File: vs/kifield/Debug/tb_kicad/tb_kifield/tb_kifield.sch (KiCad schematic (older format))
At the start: 8 parts, among them U1 R

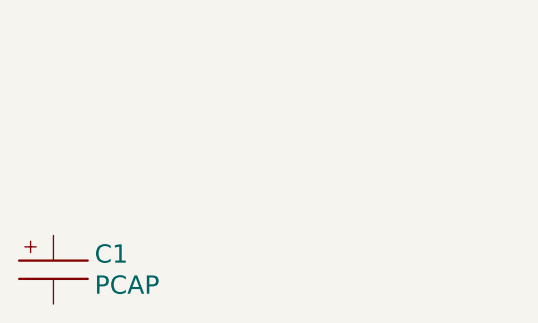
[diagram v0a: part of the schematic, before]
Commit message: Написал ReplaceAttr_text_size.bat для замены атрибута поля компонентов на 80.
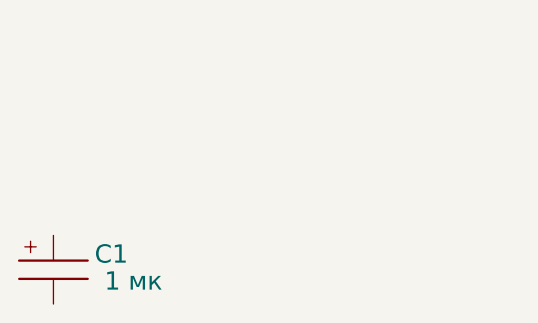
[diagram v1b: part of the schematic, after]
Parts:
- C1: Ном. - -> 1 мк
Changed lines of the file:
@@
 F 2 "-" H 9600 2085 40  0001 C CNN
 F 3 "-" H 9600 2085 40  0001 C CNN
-F 4 "-" H 9670 2085 40  0001 C CNN "Примечание"
-F 5 "-" H 9670 2085 40  0001 C CNN "Тип элемента"
-F 6 "-" H 9670 2085 40  0001 C CNN "Заказной номер "
-F 7 "-" H 9670 2085 40  0001 C CNN "Кол‐во"
-F 8 "-" H 9670 2085 40  0001 C CNN "Производитель"
-F 9 "-" H 9670 2085 40  0001 C CNN "Типоразмер"
-F 10 "-" H 9670 2085 40  0001 C CNN "Ном."
-F 11 "-" H 9670 2085 40  0001 C CNN "Откл,%"
+F 4 "-" H 9670 2085 40  0001 C CNN "Заказной номер "
+F 5 "-" H 9670 2085 40  0001 C CNN "Кол‐во"
+F 6 "-" H 9670 2085 40  0001 C CNN "Наименование 1С8 УПП"
+F 7 "-" H 9670 2085 40  0001 C CNN "Напр."
+F 8 "-" H 9670 2085 40  0001 C CNN "Ном."
+F 9 "-" H 9670 2085 40  0001 C CNN "Откл,%"
+F 10 "-" H 9670 2085 40  0001 C CNN "Примечание"
+F 11 "-" H 9670 2085 40  0001 C CNN "Производитель"
 F 12 "-" H 9670 2085 40  0001 C CNN "ТКЕ/ТКС"
-F 13 "-" H 9670 2085 40  0001 C CNN "Напр."
-F 14 "-" H 9670 2085 40  0001 C CNN "Наименование 1С8 УПП"
+F 13 "-" H 9670 2085 40  0001 C CNN "Тип элемента"
+F 14 "-" H 9670 2085 40  0001 C CNN "Типоразмер"
 	1    9600 2100
 	1    0    0    -1
@@
 F 2 "-" H 7650 2335 40  0001 C CNN
 F 3 "-" H 7650 2335 40  0001 C CNN
-F 4 "-" H 7650 2335 40  0001 C CNN "Примечание"
-F 5 "-" H 7650 2335 40  0001 C CNN "Тип элемента"
-F 6 "-" H 7650 2335 40  0001 C CNN "Заказной номер "
-F 7 "-" H 7650 2335 40  0001 C CNN "Кол‐во"
-F 8 "-" H 7650 2335 40  0001 C CNN "Производитель"
-F 9 "-" H 7650 2335 40  0001 C CNN "Типоразмер"
-F 10 "-" H 7650 2335 40  0001 C CNN "Ном."
-F 11 "-" H 7650 2335 40  0001 C CNN "Откл,%"
+F 4 "-" H 7650 2335 40  0001 C CNN "Заказной номер "
+F 5 "-" H 7650 2335 40  0001 C CNN "Кол‐во"
+F 6 "-" H 7650 2335 40  0001 C CNN "Наименование 1С8 УПП"
+F 7 "-" H 7650 2335 40  0001 C CNN "Напр."
+F 8 "-" H 7650 2335 40  0001 C CNN "Ном."
+F 9 "-" H 7650 2335 40  0001 C CNN "Откл,%"
+F 10 "-" H 7650 2335 40  0001 C CNN "Примечание"
+F 11 "-" H 7650 2335 40  0001 C CNN "Производитель"
 F 12 "-" H 7650 2335 40  0001 C CNN "ТКЕ/ТКС"
-F 13 "-" H 7650 2335 40  0001 C CNN "Напр."
-F 14 "-" H 7650 2335 40  0001 C CNN "Наименование 1С8 УПП"
+F 13 "-" H 7650 2335 40  0001 C CNN "Тип элемента"
+F 14 "-" H 7650 2335 40  0001 C CNN "Типоразмер"
 	1    7650 2350
 	1    0    0    -1
@@
 F 2 "-" H 7200 1600 30  0001 C CNN
 F 3 "-" H 7200 1600 30  0001 C CNN
-F 4 "-" H 7200 1600 30  0001 C CNN "Примечание"
-F 5 "-" H 7200 1600 30  0001 C CNN "Тип элемента"
-F 6 "-" H 7200 1600 30  0001 C CNN "Заказной номер "
-F 7 "-" H 7200 1600 30  0001 C CNN "Кол‐во"
-F 8 "-" H 7200 1600 30  0001 C CNN "Производитель"
-F 9 "-" H 7200 1600 30  0001 C CNN "Типоразмер"
-F 10 "-" H 7200 1600 30  0001 C CNN "Ном."
-F 11 "-" H 7200 1600 30  0001 C CNN "Откл,%"
+F 4 "-" H 7200 1600 30  0001 C CNN "Заказной номер "
+F 5 "-" H 7200 1600 30  0001 C CNN "Кол‐во"
+F 6 "-" H 7200 1600 30  0001 C CNN "Наименование 1С8 УПП"
+F 7 "-" H 7200 1600 30  0001 C CNN "Напр."
+F 8 "-" H 7200 1600 30  0001 C CNN "Ном."
+F 9 "-" H 7200 1600 30  0001 C CNN "Откл,%"
+F 10 "-" H 7200 1600 30  0001 C CNN "Примечание"
+F 11 "-" H 7200 1600 30  0001 C CNN "Производитель"
 F 12 "-" H 7200 1600 30  0001 C CNN "ТКЕ/ТКС"
-F 13 "-" H 7200 1600 30  0001 C CNN "Напр."
-F 14 "-" H 7200 1600 30  0001 C CNN "Наименование 1С8 УПП"
+F 13 "-" H 7200 1600 30  0001 C CNN "Тип элемента"
+F 14 "-" H 7200 1600 30  0001 C CNN "Типоразмер"
 	1    7200 1650
 	1    0    0    -1
@@
 F 2 "-" H 5600 1100 30  0001 C CNN
 F 3 "-" H 5600 1100 30  0001 C CNN
-F 4 "-" H 5600 1100 30  0001 C CNN "Примечание"
-F 5 "-" H 5600 1100 30  0001 C CNN "Тип элемента"
-F 6 "-" H 5600 1100 30  0001 C CNN "Заказной номер "
-F 7 "-" H 5600 1100 30  0001 C CNN "Кол‐во"
-F 8 "-" H 5600 1100 30  0001 C CNN "Производитель"
-F 9 "-" H 5600 1100 30  0001 C CNN "Типоразмер"
-F 10 "-" H 5600 1100 30  0001 C CNN "Ном."
-F 11 "-" H 5600 1100 30  0001 C CNN "Откл,%"
+F 4 "-" H 5600 1100 30  0001 C CNN "Заказной номер "
+F 5 "-" H 5600 1100 30  0001 C CNN "Кол‐во"
+F 6 "-" H 5600 1100 30  0001 C CNN "Наименование 1С8 УПП"
+F 7 "-" H 5600 1100 30  0001 C CNN "Напр."
+F 8 "-" H 5600 1100 30  0001 C CNN "Ном."
+F 9 "-" H 5600 1100 30  0001 C CNN "Откл,%"
+F 10 "-" H 5600 1100 30  0001 C CNN "Примечание"
+F 11 "-" H 5600 1100 30  0001 C CNN "Производитель"
 F 12 "-" H 5600 1100 30  0001 C CNN "ТКЕ/ТКС"
-F 13 "-" H 5600 1100 30  0001 C CNN "Напр."
-F 14 "-" H 5600 1100 30  0001 C CNN "Наименование 1С8 УПП"
+F 13 "-" H 5600 1100 30  0001 C CNN "Тип элемента"
+F 14 "-" H 5600 1100 30  0001 C CNN "Типоразмер"
 	1    5600 1500
 	1    0    0    -1
@@
 F 2 "-" H 7550 3350 30  0001 C CNN
 F 3 "-" H 7550 3350 30  0001 C CNN
-F 4 "-" H 7550 3350 30  0001 C CNN "Примечание"
-F 5 "-" H 7550 3350 30  0001 C CNN "Тип элемента"
-F 6 "-" H 7550 3350 30  0001 C CNN "Заказной номер "
-F 7 "-" H 7550 3350 30  0001 C CNN "Кол‐во"
-F 8 "-" H 7550 3350 30  0001 C CNN "Производитель"
-F 9 "-" H 7550 3350 30  0001 C CNN "Типоразмер"
-F 10 "-" H 7550 3350 30  0001 C CNN "Ном."
-F 11 "-" H 7550 3350 30  0001 C CNN "Откл,%"
+F 4 "-" H 7550 3350 30  0001 C CNN "Заказной номер "
+F 5 "-" H 7550 3350 30  0001 C CNN "Кол‐во"
+F 6 "-" H 7550 3350 30  0001 C CNN "Наименование 1С8 УПП"
+F 7 "-" H 7550 3350 30  0001 C CNN "Напр."
+F 8 "-" H 7550 3350 30  0001 C CNN "Ном."
+F 9 "-" H 7550 3350 30  0001 C CNN "Откл,%"
+F 10 "-" H 7550 3350 30  0001 C CNN "Примечание"
+F 11 "-" H 7550 3350 30  0001 C CNN "Производитель"
 F 12 "-" H 7550 3350 30  0001 C CNN "ТКЕ/ТКС"
-F 13 "-" H 7550 3350 30  0001 C CNN "Напр."
-F 14 "-" H 7550 3350 30  0001 C CNN "Наименование 1С8 УПП"
+F 13 "-" H 7550 3350 30  0001 C CNN "Тип элемента"
+F 14 "-" H 7550 3350 30  0001 C CNN "Типоразмер"
 	1    7550 3400
 	1    0    0    -1
@@
 P 2350 4150
 F 0 "C1" H 2530 4218 80  0000 L CNN
-F 1 "PCAP" H 2530 4082 80  0000 L CNN
+F 1 "PCAP" H 2530 4082 80  0001 L CNN
 F 2 "-" H 2350 4135 40  0001 C CNN
 F 3 "-" H 2350 4135 40  0001 C CNN
-F 4 "-" H 2420 4135 40  0001 C CNN "Примечание"
-F 5 "-" H 2420 4135 40  0001 C CNN "Тип элемента"
-F 6 "-" H 2420 4135 40  0001 C CNN "Заказной номер "
-F 7 "-" H 2420 4135 40  0001 C CNN "Кол‐во"
-F 8 "-" H 2420 4135 40  0001 C CNN "Производитель"
-F 9 "-" H 2420 4135 40  0001 C CNN "Типоразмер"
-F 10 "-" H 2420 4135 40  0001 C CNN "Ном."
-F 11 "-" H 2420 4135 40  0001 C CNN "Откл,%"
+F 4 "-" H 2420 4135 40  0001 C CNN "Заказной номер "
+F 5 "-" H 2420 4135 40  0001 C CNN "Кол‐во"
+F 6 "-" H 2420 4135 40  0001 C CNN "Наименование 1С8 УПП"
+F 7 "-" H 2420 4135 40  0001 C CNN "Напр."
+F 8 "1 мк" H 2700 4100 80  0000 C CNN "Ном."
+F 9 "-" H 2420 4135 40  0001 C CNN "Откл,%"
+F 10 "-" H 2420 4135 40  0001 C CNN "Примечание"
+F 11 "-" H 2420 4135 40  0001 C CNN "Производитель"
 F 12 "-" H 2420 4135 40  0001 C CNN "ТКЕ/ТКС"
-F 13 "-" H 2420 4135 40  0001 C CNN "Напр."
-F 14 "-" H 2420 4135 40  0001 C CNN "Наименование 1С8 УПП"
+F 13 "-" H 2420 4135 40  0001 C CNN "Тип элемента"
+F 14 "-" H 2420 4135 40  0001 C CNN "Типоразмер"
 	1    2350 4150
 	1    0    0    -1
@@
 F 2 "-" H 3000 1800 30  0001 C CNN
 F 3 "-" H 3000 1800 30  0001 C CNN
-F 4 "-" H 3000 1800 30  0001 C CNN "Примечание"
-F 5 "-" H 3000 1800 30  0001 C CNN "Тип элемента"
-F 6 "-" H 3000 1800 30  0001 C CNN "Заказной номер "
-F 7 "-" H 3000 1800 30  0001 C CNN "Кол‐во"
-F 8 "-" H 3000 1800 30  0001 C CNN "Производитель"
-F 9 "-" H 3000 1800 30  0001 C CNN "Типоразмер"
-F 10 "-" H 3000 1800 30  0001 C CNN "Ном."
-F 11 "-" H 3000 1800 30  0001 C CNN "Откл,%"
+F 4 "-" H 3000 1800 30  0001 C CNN "Заказной номер "
+F 5 "-" H 3000 1800 30  0001 C CNN "Кол‐во"
+F 6 "-" H 3000 1800 30  0001 C CNN "Наименование 1С8 УПП"
+F 7 "-" H 3000 1800 30  0001 C CNN "Напр."
+F 8 "-" H 3000 1800 30  0001 C CNN "Ном."
+F 9 "-" H 3000 1800 30  0001 C CNN "Откл,%"
+F 10 "-" H 3000 1800 30  0001 C CNN "Примечание"
+F 11 "-" H 3000 1800 30  0001 C CNN "Производитель"
 F 12 "-" H 3000 1800 30  0001 C CNN "ТКЕ/ТКС"
-F 13 "-" H 3000 1800 30  0001 C CNN "Напр."
-F 14 "-" H 3000 1800 30  0001 C CNN "Наименование 1С8 УПП"
+F 13 "-" H 3000 1800 30  0001 C CNN "Тип элемента"
+F 14 "-" H 3000 1800 30  0001 C CNN "Типоразмер"
 	1    3000 1850
 	1    0    0    -1
@@
 F 2 "-" H 4000 2400 30  0001 C CNN
 F 3 "-" H 4000 2400 30  0001 C CNN
-F 4 "-" H 4000 2400 30  0001 C CNN "Примечание"
-F 5 "-" H 4000 2400 30  0001 C CNN "Тип элемента"
-F 6 "-" H 4000 2400 30  0001 C CNN "Заказной номер "
-F 7 "-" H 4000 2400 30  0001 C CNN "Кол‐во"
-F 8 "-" H 4000 2400 30  0001 C CNN "Производитель"
-F 9 "-" H 4000 2400 30  0001 C CNN "Типоразмер"
-F 10 "-" H 4000 2400 30  0001 C CNN "Ном."
-F 11 "-" H 4000 2400 30  0001 C CNN "Откл,%"
+F 4 "-" H 4000 2400 30  0001 C CNN "Заказной номер "
+F 5 "-" H 4000 2400 30  0001 C CNN "Кол‐во"
+F 6 "-" H 4000 2400 30  0001 C CNN "Наименование 1С8 УПП"
+F 7 "-" H 4000 2400 30  0001 C CNN "Напр."
+F 8 "-" H 4000 2400 30  0001 C CNN "Ном."
+F 9 "-" H 4000 2400 30  0001 C CNN "Откл,%"
+F 10 "-" H 4000 2400 30  0001 C CNN "Примечание"
+F 11 "-" H 4000 2400 30  0001 C CNN "Производитель"
 F 12 "-" H 4000 2400 30  0001 C CNN "ТКЕ/ТКС"
-F 13 "-" H 4000 2400 30  0001 C CNN "Напр."
-F 14 "-" H 4000 2400 30  0001 C CNN "Наименование 1С8 УПП"
+F 13 "-" H 4000 2400 30  0001 C CNN "Тип элемента"
+F 14 "-" H 4000 2400 30  0001 C CNN "Типоразмер"
 	1    4000 2450
 	1    0    0    -1

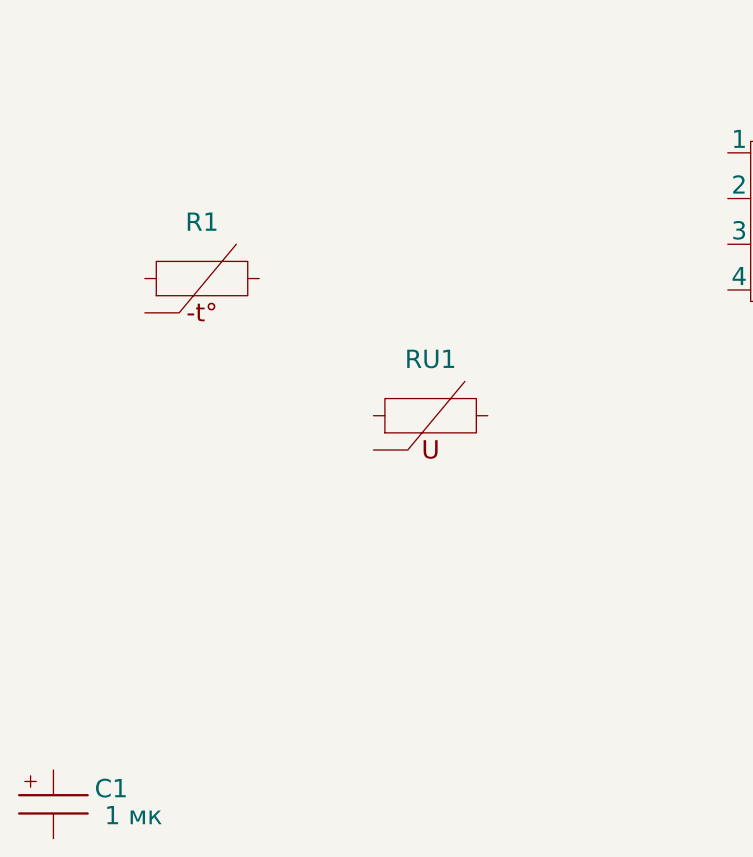
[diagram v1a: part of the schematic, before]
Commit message: Отладил ReplaceAttr_text_size.bat. Необходимо провести замены в файле Sch.tsv Refs -> Поз.обозначение value -> Наименование
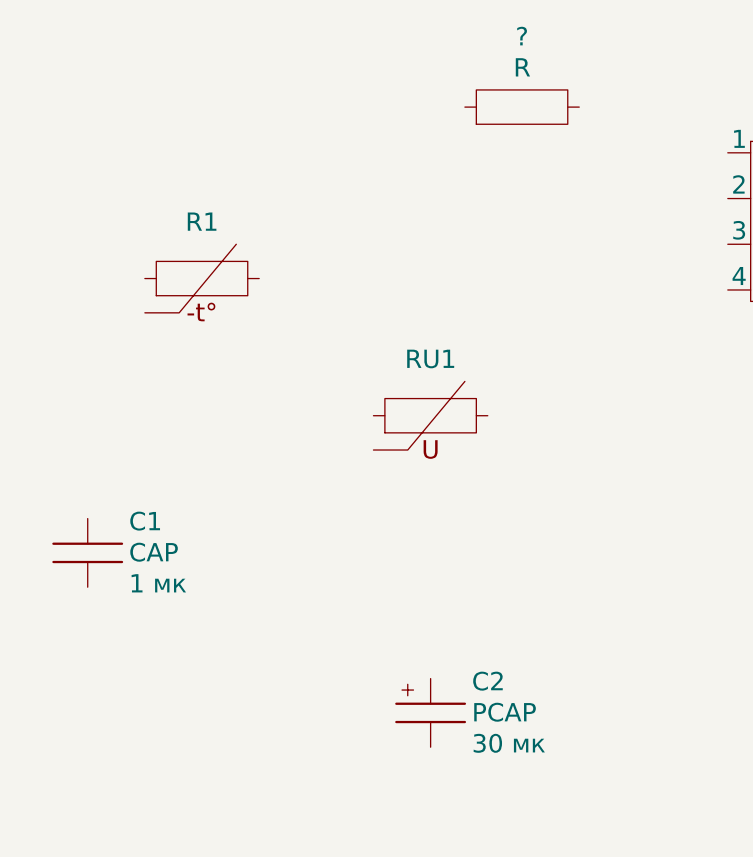
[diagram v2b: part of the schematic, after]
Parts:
- removed C1: PCAP, -, symbol Capacity:PCAP
- added ?: R, -, symbol Resistors:R
- added C1: CAP, -, symbol Capacity:CAP
- added C2: PCAP, -, symbol Capacity:PCAP
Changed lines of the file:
@@
-$EndComp
-$Comp
-L Capacity:PCAP C1
-U 1 1 5F918A9B
-P 2350 4150
-F 0 "C1" H 2530 4218 80  0000 L CNN
-F 1 "PCAP" H 2530 4082 80  0001 L CNN
-F 2 "-" H 2350 4135 40  0001 C CNN
-F 3 "-" H 2350 4135 40  0001 C CNN
-F 4 "-" H 2420 4135 40  0001 C CNN "Заказной номер "
-F 5 "-" H 2420 4135 40  0001 C CNN "Кол‐во"
-F 6 "-" H 2420 4135 40  0001 C CNN "Наименование 1С8 УПП"
-F 7 "-" H 2420 4135 40  0001 C CNN "Напр."
-F 8 "1 мк" H 2700 4100 80  0000 C CNN "Ном."
-F 9 "-" H 2420 4135 40  0001 C CNN "Откл,%"
-F 10 "-" H 2420 4135 40  0001 C CNN "Примечание"
-F 11 "-" H 2420 4135 40  0001 C CNN "Производитель"
-F 12 "-" H 2420 4135 40  0001 C CNN "ТКЕ/ТКС"
-F 13 "-" H 2420 4135 40  0001 C CNN "Тип элемента"
-F 14 "-" H 2420 4135 40  0001 C CNN "Типоразмер"
-	1    2350 4150
-	1    0    0    -1
 $EndComp
 $Comp
@@
 F 0 "RU1" H 4000 2696 80  0000 C CNN
 F 1 "RU" H 4000 2200 80  0001 C CNN
-F 2 "-" H 4000 2400 30  0001 C CNN
-F 3 "-" H 4000 2400 30  0001 C CNN
-F 4 "-" H 4000 2400 30  0001 C CNN "Заказной номер "
-F 5 "-" H 4000 2400 30  0001 C CNN "Кол‐во"
-F 6 "-" H 4000 2400 30  0001 C CNN "Наименование 1С8 УПП"
-F 7 "-" H 4000 2400 30  0001 C CNN "Напр."
-F 8 "-" H 4000 2400 30  0001 C CNN "Ном."
-F 9 "-" H 4000 2400 30  0001 C CNN "Откл,%"
-F 10 "-" H 4000 2400 30  0001 C CNN "Примечание"
-F 11 "-" H 4000 2400 30  0001 C CNN "Производитель"
-F 12 "-" H 4000 2400 30  0001 C CNN "ТКЕ/ТКС"
-F 13 "-" H 4000 2400 30  0001 C CNN "Тип элемента"
-F 14 "-" H 4000 2400 30  0001 C CNN "Типоразмер"
+F 2 "-" H 4000 2400 80  0001 C CNN
+F 3 "-" H 4000 2400 80  0001 C CNN
+F 4 "-" H 4000 2400 80  0001 C CNN "Заказной номер "
+F 5 "-" H 4000 2400 80  0001 C CNN "Кол‐во"
+F 6 "-" H 4000 2400 80  0001 C CNN "Наименование 1С8 УПП"
+F 7 "-" H 4000 2400 80  0001 C CNN "Напр."
+F 8 "-" H 4000 2400 80  0001 C CNN "Ном."
+F 9 "-" H 4000 2400 80  0001 C CNN "Откл,%"
+F 10 "-" H 4000 2400 80  0001 C CNN "Примечание"
+F 11 "-" H 4000 2400 80  0001 C CNN "Производитель"
+F 12 "-" H 4000 2400 80  0001 C CNN "ТКЕ/ТКС"
+F 13 "-" H 4000 2400 80  0001 C CNN "Тип элемента"
+F 14 "-" H 4000 2400 80  0001 C CNN "Типоразмер"
 	1    4000 2450
 	1    0    0    -1
 $EndComp
+$Comp
+L Capacity:CAP C1
+U 1 1 5F92A78F
+P 2500 3050
+F 0 "C1" H 2680 3186 80  0000 L CNN
+F 1 "CAP" H 2680 3050 80  0000 L CNN
+F 2 "-" H 2500 3035 80  0001 C CNN
+F 3 "-" H 2500 3035 80  0001 C CNN
+F 4 "-" H 2500 3035 80  0001 C CNN "Примечание"
+F 5 "-" H 2500 3035 80  0001 C CNN "Тип элемента"
+F 6 "-" H 2500 3035 80  0001 C CNN "Заказной номер "
+F 7 "-" H 2500 3035 80  0001 C CNN "Кол‐во"
+F 8 "-" H 2500 3035 80  0001 C CNN "Производитель"
+F 9 "-" H 2500 3035 80  0001 C CNN "Типоразмер"
+F 10 "1 мк" H 2680 2914 80  0000 L CNN "Ном."
+F 11 "-" H 2500 3035 80  0001 C CNN "Откл,%"
+F 12 "-" H 2500 3035 80  0001 C CNN "ТКЕ/ТКС"
+F 13 "-" H 2500 3035 80  0001 C CNN "Напр."
+F 14 "-" H 2500 3035 80  0001 C CNN "Наименование 1С8 УПП"
+	1    2500 3050
+	1    0    0    -1
+$EndComp
+$Comp
+L Capacity:PCAP C2
+U 1 1 5F92BADC
+P 4000 3750
+F 0 "C2" H 4180 3886 80  0000 L CNN
+F 1 "PCAP" H 4180 3750 80  0000 L CNN
+F 2 "-" H 4000 3735 80  0001 C CNN
+F 3 "-" H 4000 3735 80  0001 C CNN
+F 4 "-" H 4070 3735 80  0001 C CNN "Примечание"
+F 5 "-" H 4070 3735 80  0001 C CNN "Тип элемента"
+F 6 "-" H 4070 3735 80  0001 C CNN "Заказной номер "
+F 7 "-" H 4070 3735 80  0001 C CNN "Кол‐во"
+F 8 "-" H 4070 3735 80  0001 C CNN "Производитель"
+F 9 "-" H 4070 3735 80  0001 C CNN "Типоразмер"
+F 10 "30 мк" H 4180 3614 80  0000 L CNN "Ном."
+F 11 "-" H 4070 3735 80  0001 C CNN "Откл,%"
+F 12 "-" H 4070 3735 80  0001 C CNN "ТКЕ/ТКС"
+F 13 "-" H 4070 3735 80  0001 C CNN "Напр."
+F 14 "-" H 4070 3735 80  0001 C CNN "Наименование 1С8 УПП"
+	1    4000 3750
+	1    0    0    -1
+$EndComp
+$Comp
+L Resistors:R ?
+U 1 1 5F92EE67
+P 4400 1100
+F 0 "?" H 4400 1407 80  0000 C CNN
+F 1 "R" H 4400 1271 80  0000 C CNN
+F 2 "-" H 4400 1050 80  0001 C CNN
+F 3 "-" H 4400 1050 80  0001 C CNN
+F 4 "-" H 4400 1050 80  0001 C CNN "Примечание"
+F 5 "-" H 4400 1050 80  0001 C CNN "Тип элемента"
+F 6 "-" H 4400 1050 80  0001 C CNN "Заказной номер "
+F 7 "-" H 4400 1050 80  0001 C CNN "Кол‐во"
+F 8 "-" H 4400 1050 80  0001 C CNN "Производитель"
+F 9 "-" H 4400 1050 80  0001 C CNN "Типоразмер"
+F 10 "-" H 4400 1050 80  0001 C CNN "Ном."
+F 11 "-" H 4400 1050 80  0001 C CNN "Откл,%"
+F 12 "-" H 4400 1050 80  0001 C CNN "ТКЕ/ТКС"
+F 13 "-" H 4400 1050 80  0001 C CNN "Напр."
+F 14 "-" H 4400 1050 80  0001 C CNN "Наименование 1С8 УПП"
+	1    4400 1100
+	1    0    0    -1
+$EndComp

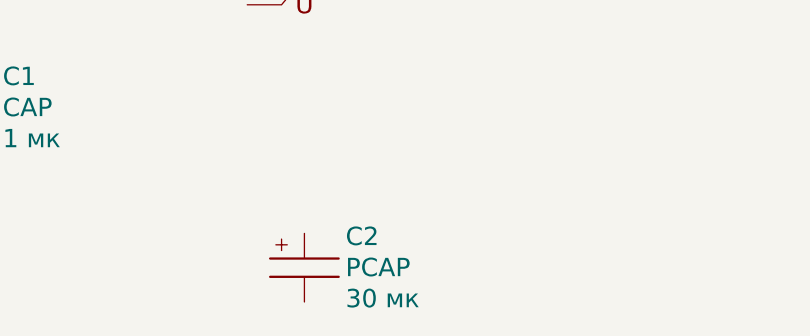
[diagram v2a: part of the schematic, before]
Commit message: Отладил работу батников sch2tsv.bat/tsv2sch.bat. Добавлена возможность подмены полей Refs/Value на Поз.обозначение/Наименование в tsv файле.
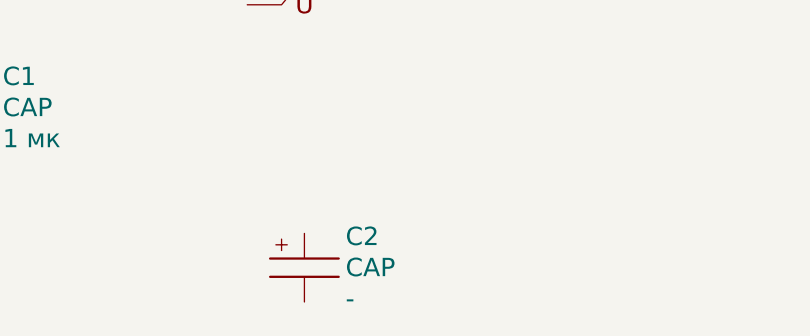
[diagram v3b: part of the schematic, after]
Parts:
- C2: value PCAP -> CAP; Ном. 30 мк -> -
- C3: Производитель - -> 5
- R1: Ном. - -> 1 Ом; Производитель - -> 6
- R2: Ном. - -> 2 Ом; Производитель - -> 7
- R3: Ном. - -> 3 Ом; Производитель - -> 8

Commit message: Поправили идеологию использования элементов для СП в части материалов - см.KiCAD_Fields.xlsx. Необходимо запускать скрипты из kicad.
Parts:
- added MAT1: Wire, FOOTPRINT:mat_wire, symbol !PROJECT:Wire
- added MAT2: Tube, symbol !PROJECT:Tube
- gave numbers to parts that had none: 1
- renumbered C2 to C1, C1 to C2, C2 to C3, C3 to C4, R2 to R3, R3 to R4
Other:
- moved on the sheet: C1

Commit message: Написал sch2tsv_KiCAD.bat/tsv2sch__KiCAD.bat для использования в качестве скриптов в KiCAD->Eechema->Инструменты->Сформировать перечень элементов. 1. Скопировать   sch2tsv_KiCAD.bat, tsv2sch__KiCAD.bat, sch2tsv.sed, tsv2sch.sed. 2. Добавить в KiCAD->Eechema->Инструменты->Сформировать перечень элементов: sch2tsv Команда: D:\KiCAD_FIVE_LIBS\SCRIPT\sch2tsv_KiCAD.bat "%I" tsv2sch Команда: D:\KiCAD_FIVE_LIBS\SCRIPT\tsv2sch__KiCAD.bat "%I"
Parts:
- R2: Ном. - -> 35

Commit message: Перенес батнички из проекта KiCAD в отдельный файл.
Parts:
- R2: Ном. 35 -> 99
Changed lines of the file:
@@
 F 6 "-" H 4400 1050 80 0001 C CNN "Наименование 1С8 УПП"
 F 7 "-" H 4400 1050 80 0001 C CNN "Напр."
-F 8 "35" H 4400 1050 80 0001 C CNN "Ном."
+F 8 "99" H 4400 1050 80 0001 C CNN "Ном."
 F 9 "-" H 4400 1050 80 0001 C CNN "Откл,%"
 F 10 "-" H 4400 1050 80 0001 C CNN "Примечание"

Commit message: kifield-0.1.24 - добавил принудительную установку поля text_size в значение 80 для вновь добавляемых компонентов.
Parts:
- removed C1, C2: CAP, -, symbol Capacity:CAP
- removed C3: CAP, -, symbol Capacity:PCAP
- removed C4: PCAP, -, symbol Capacity:PCAP
- removed MAT1: Wire, FOOTPRINT:mat_wire, symbol !PROJECT:Wire
- removed MAT2: Tube, symbol !PROJECT:Tube
- removed R1: RT, -, symbol Resistors:RT
- removed R2, U1: R, -, symbol Resistors:R
- removed R3: R4, -, symbol Resistors:R4
- removed R4: RVAR, -, symbol Resistors:RVAR
- removed RU1: RU, -, symbol Resistors:RU
- added C1, C2: Capacity_PCAP, -, symbol !PROJECT:Capacity_PCAP
- added R41, R42: Resistors_R4, -, symbol !PROJECT:Resistors_R4
